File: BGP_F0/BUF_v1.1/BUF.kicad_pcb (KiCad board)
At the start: 2 copper layers, 32 x 26 mm, 33 parts, among them P1 CONN_01X02, P2 CONN_01X02, P3 CONN_01X03, P4 CONN_01X02, P5 CONN_01X09, P6 CONN_01X05, P7 CONN_01X02, Q1 2N5457, Q2 2N5457, U1 MC33178

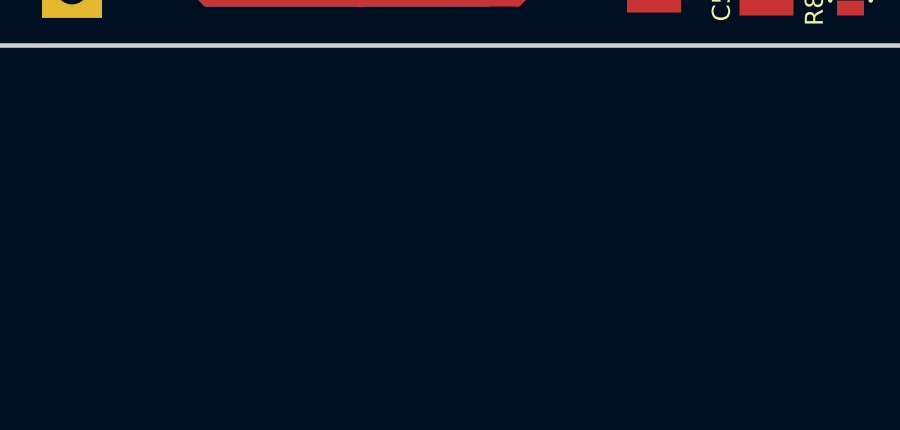
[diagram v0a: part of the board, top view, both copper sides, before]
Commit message: Some changes to names
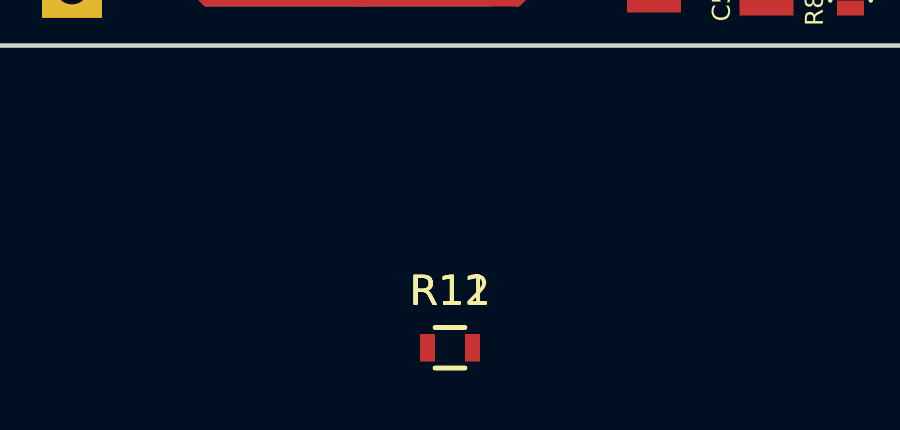
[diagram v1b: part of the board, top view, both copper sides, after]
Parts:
- added R11: 10k, Resistors_SMD:R_0603, F.Cu at (141.0, 114.1)
- added R12: 12k, Resistors_SMD:R_0603, F.Cu at (141.0, 114.1)
- C6: value 100p -> 270p
- R10: value 100 -> 1k
- R5, R6: value 49.9k -> 47k
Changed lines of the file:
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@@
 (kicad_pcb (version 4) (host pcbnew 4.0.4-1.fc24-product)
   (general
-    (links 61)
-    (no_connects 0)
-    (area 123.10412 74.549999 157.175001 104.183001)
+    (links 65)
+    (no_connects 4)
+    (area 124.924999 77.924999 157.075001 104.075001)
     (thickness 1.2)
     (drawings 8)
     (tracks 171)
     (zones 0)
-    (modules 33)
+    (modules 35)
     (nets 25)
   )
@@
       (effects (font (size 0.6 0.6) (thickness 0.15)) (justify mirror))
     )
-    (fp_text value 100p (at 0 -1.9 180) (layer B.Fab) hide
+    (fp_text value 270p (at 0 -1.9 180) (layer B.Fab) hide
       (effects (font (size 0.6 0.6) (thickness 0.15)) (justify mirror))
     )
@@
       (effects (font (size 0.6 0.6) (thickness 0.15)) (justify mirror))
     )
-    (fp_text value 49.9k (at 0 -1.9) (layer B.Fab) hide
+    (fp_text value 47k (at 0 -1.9) (layer B.Fab) hide
       (effects (font (size 0.6 0.6) (thickness 0.15)) (justify mirror))
     )
@@
       (effects (font (size 0.6 0.6) (thickness 0.15)) (justify mirror))
     )
-    (fp_text value 49.9k (at 0 -1.9) (layer B.Fab) hide
+    (fp_text value 47k (at 0 -1.9) (layer B.Fab) hide
       (effects (font (size 0.6 0.6) (thickness 0.15)) (justify mirror))
     )
@@
       (effects (font (size 0.6 0.6) (thickness 0.15)))
     )
-    (fp_text value 100 (at 0 1.9 180) (layer F.Fab) hide
+    (fp_text value 1k (at 0 1.9 180) (layer F.Fab) hide
       (effects (font (size 0.6 0.6) (thickness 0.15)))
     )
@@
     (model Resistors_SMD.3dshapes/R_0603.wrl
       (at (xyz 0 0 0))
+      (scale (xyz 1 1 1))
+      (rotate (xyz 0 0 0))
+    )
+  )
+  (module Resistors_SMD:R_0603 (layer F.Cu)
+    (at 141 114.075001)
+    (descr "Resistor SMD 0603, reflow soldering, Vishay (see dcrcw.pdf)")
+    (tags "resistor 0603")
+    (attr smd)
+    (fp_text reference R11 (at 0 -1.9) (layer F.SilkS)
+      (effects (font (size 1 1) (thickness 0.15)))
+    )
+    (fp_text value 10k (at 0 1.9) (layer F.Fab)
+      (effects (font (size 1 1) (thickness 0.15)))
+    )
+    (fp_line (start -1.3 -0.8) (end 1.3 -0.8) (layer F.CrtYd) (width 0.05))
+    (fp_line (start -1.3 0.8) (end 1.3 0.8) (layer F.CrtYd) (width 0.05))
+    (fp_line (start -1.3 -0.8) (end -1.3 0.8) (layer F.CrtYd) (width 0.05))
+    (fp_line (start 1.3 -0.8) (end 1.3 0.8) (layer F.CrtYd) (width 0.05))
+    (fp_line (start 0.5 0.675) (end -0.5 0.675) (layer F.SilkS) (width 0.15))
+    (fp_line (start -0.5 -0.675) (end 0.5 -0.675) (layer F.SilkS) (width 0.15))
+    (pad 1 smd rect (at -0.75 0) (size 0.5 0.9) (layers F.Cu F.Paste F.Mask)
+      (net 11 /PV_3))
+    (pad 2 smd rect (at 0.75 0) (size 0.5 0.9) (layers F.Cu F.Paste F.Mask)
+      (net 14 /PV_2))
+    (model Resistors_SMD.3dshapes/R_0603.wrl
+      (at (xyz 0 0 0))
+      (scale (xyz 1 1 1))
+      (rotate (xyz 0 0 0))
+    )
+  )
+  (module Resistors_SMD:R_0603 (layer F.Cu)
+    (at 141 114.075001)
+    (descr "Resistor SMD 0603, reflow soldering, Vishay (see dcrcw.pdf)")
+    (tags "resistor 0603")
+    (attr smd)
+    (fp_text reference R12 (at 0 -1.9) (layer F.SilkS)
+      (effects (font (size 1 1) (thickness 0.15)))
+    )
+    (fp_text value 12k (at 0 1.9) (layer F.Fab)
+      (effects (font (size 1 1) (thickness 0.15)))
+    )
+    (fp_line (start -1.3 -0.8) (end 1.3 -0.8) (layer F.CrtYd) (width 0.05))
+    (fp_line (start -1.3 0.8) (end 1.3 0.8) (layer F.CrtYd) (width 0.05))
+    (fp_line (start -1.3 -0.8) (end -1.3 0.8) (layer F.CrtYd) (width 0.05))
+    (fp_line (start 1.3 -0.8) (end 1.3 0.8) (layer F.CrtYd) (width 0.05))
+    (fp_line (start 0.5 0.675) (end -0.5 0.675) (layer F.SilkS) (width 0.15))
+    (fp_line (start -0.5 -0.675) (end 0.5 -0.675) (layer F.SilkS) (width 0.15))
+    (pad 1 smd rect (at -0.75 0) (size 0.5 0.9) (layers F.Cu F.Paste F.Mask)
+      (net 14 /PV_2))
+    (pad 2 smd rect (at 0.75 0) (size 0.5 0.9) (layers F.Cu F.Paste F.Mask)
+      (net 8 Earth))
+    (model Resistors_SMD.3dshapes/R_0603.wrl
+      (at (xyz 0 0 0))

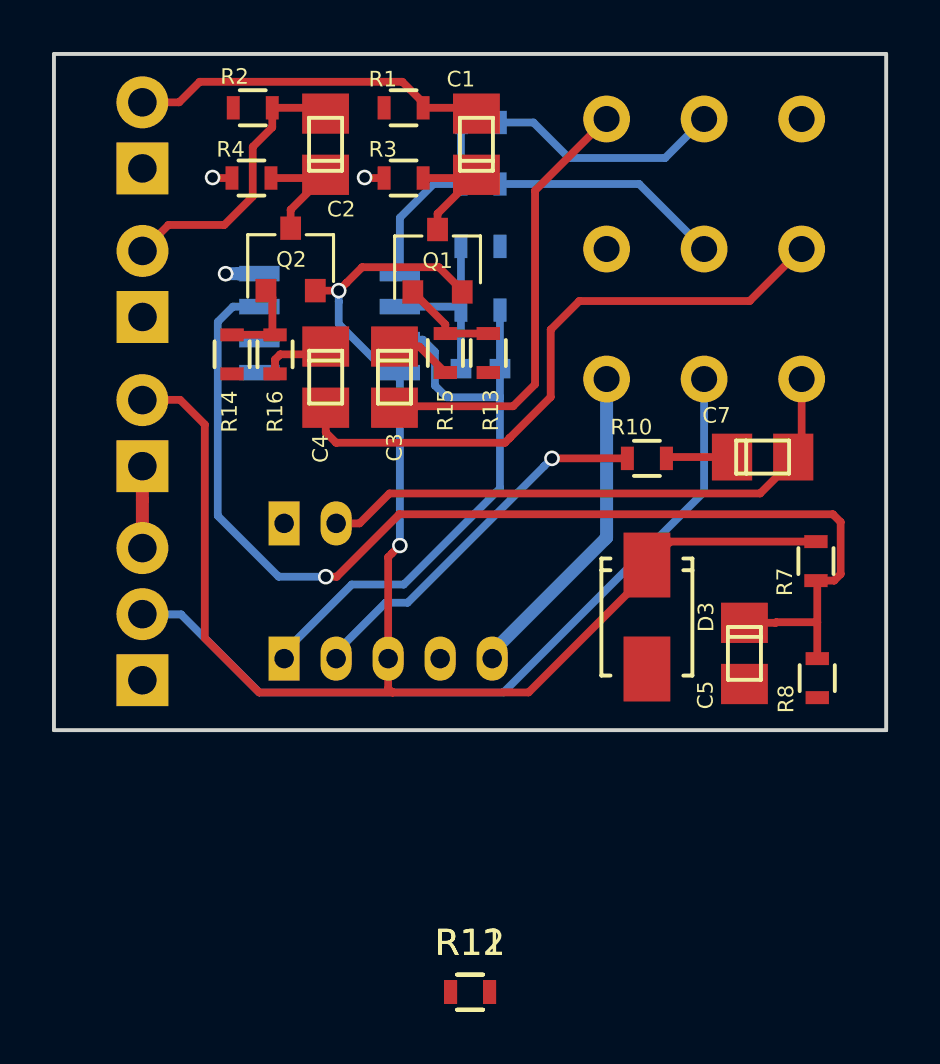
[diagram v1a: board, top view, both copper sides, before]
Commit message: F0 - Fixed Mid Stack, BT, BUF
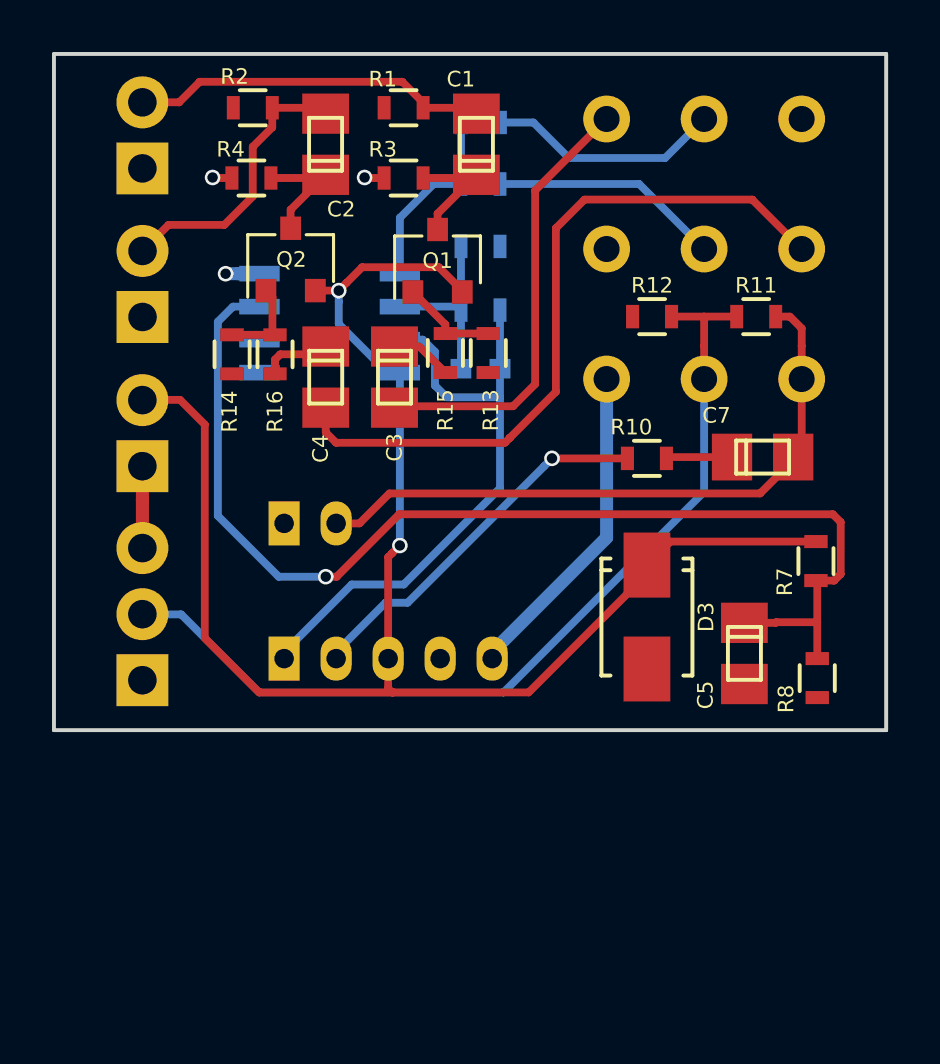
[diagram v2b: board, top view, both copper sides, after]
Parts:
- moved R11 28.2 mm to (152.0, 88.1), turned to 180 degrees
- moved R12 26.9 mm to (148.0, 88.1), turned to 180 degrees
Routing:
- net /PV_2: track 30.4 -> 35.3 mm
- net /PB2_3: track 24.1 -> 27.8 mm
- net /PV_3: track 22.2 -> 25.3 mm
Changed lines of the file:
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@@
-(kicad_pcb (version 4) (host pcbnew 4.0.4-1.fc24-product)
+(kicad_pcb (version 4) (host pcbnew 4.0.7)
   (general
     (links 65)
-    (no_connects 4)
+    (no_connects 0)
     (area 124.924999 77.924999 157.075001 104.075001)
     (thickness 1.2)
     (drawings 8)
-    (tracks 171)
+    (tracks 179)
     (zones 0)
     (modules 35)
@@
     (add_net "Net-(R5-Pad1)")
   )
+  (module Resistors_SMD:R_0603 (layer F.Cu)
+    (at 152 88.1 180)
+    (descr "Resistor SMD 0603, reflow soldering, Vishay (see dcrcw.pdf)")
+    (tags "resistor 0603")
+    (attr smd)
+    (fp_text reference R11 (at 0 1.2 180) (layer F.SilkS)
+      (effects (font (size 0.6 0.6) (thickness 0.15)))
+    )
+    (fp_text value 10k (at 0 1.9 180) (layer F.Fab) hide
+      (effects (font (size 0.6 0.6) (thickness 0.15)))
+    )
+    (fp_line (start -1.3 -0.8) (end 1.3 -0.8) (layer F.CrtYd) (width 0.05))
+    (fp_line (start -1.3 0.8) (end 1.3 0.8) (layer F.CrtYd) (width 0.05))
+    (fp_line (start -1.3 -0.8) (end -1.3 0.8) (layer F.CrtYd) (width 0.05))
+    (fp_line (start 1.3 -0.8) (end 1.3 0.8) (layer F.CrtYd) (width 0.05))
+    (fp_line (start 0.5 0.675) (end -0.5 0.675) (layer F.SilkS) (width 0.15))
+    (fp_line (start -0.5 -0.675) (end 0.5 -0.675) (layer F.SilkS) (width 0.15))
+    (pad 1 smd rect (at -0.75 0 180) (size 0.5 0.9) (layers F.Cu F.Paste F.Mask)
+      (net 11 /PV_3))
+    (pad 2 smd rect (at 0.75 0 180) (size 0.5 0.9) (layers F.Cu F.Paste F.Mask)
+      (net 14 /PV_2))
+    (model Resistors_SMD.3dshapes/R_0603.wrl
+      (at (xyz 0 0 0))
+      (scale (xyz 1 1 1))
+      (rotate (xyz 0 0 0))
+    )
+  )
+  (module Resistors_SMD:R_0603 (layer F.Cu)
+    (at 148 88.1 180)
+    (descr "Resistor SMD 0603, reflow soldering, Vishay (see dcrcw.pdf)")
+    (tags "resistor 0603")
+    (attr smd)
+    (fp_text reference R12 (at 0 1.2 180) (layer F.SilkS)
+      (effects (font (size 0.6 0.6) (thickness 0.15)))
+    )
+    (fp_text value 12k (at 0 1.9 180) (layer F.Fab) hide
+      (effects (font (size 0.6 0.6) (thickness 0.15)))
+    )
+    (fp_line (start -1.3 -0.8) (end 1.3 -0.8) (layer F.CrtYd) (width 0.05))
+    (fp_line (start -1.3 0.8) (end 1.3 0.8) (layer F.CrtYd) (width 0.05))
+    (fp_line (start -1.3 -0.8) (end -1.3 0.8) (layer F.CrtYd) (width 0.05))
+    (fp_line (start 1.3 -0.8) (end 1.3 0.8) (layer F.CrtYd) (width 0.05))
+    (fp_line (start 0.5 0.675) (end -0.5 0.675) (layer F.SilkS) (width 0.15))
+    (fp_line (start -0.5 -0.675) (end 0.5 -0.675) (layer F.SilkS) (width 0.15))
+    (pad 1 smd rect (at -0.75 0 180) (size 0.5 0.9) (layers F.Cu F.Paste F.Mask)
+      (net 14 /PV_2))
+    (pad 2 smd rect (at 0.75 0 180) (size 0.5 0.9) (layers F.Cu F.Paste F.Mask)
+      (net 8 Earth))
+    (model Resistors_SMD.3dshapes/R_0603.wrl
+      (at (xyz 0 0 0))
+      (scale (xyz 1 1 1))
+      (rotate (xyz 0 0 0))
+    )
+  )
   (module LIBS:Potentiometer_Alpha_Tripple_Vertical_Dual_Shaft (layer B.Cu)
     (at 146.25 80.5 90)
@@
     )
   )
-  (module Resistors_SMD:R_0603 (layer F.Cu)
-    (at 141 114.075001)
-    (descr "Resistor SMD 0603, reflow soldering, Vishay (see dcrcw.pdf)")
-    (tags "resistor 0603")
-    (attr smd)
-    (fp_text reference R11 (at 0 -1.9) (layer F.SilkS)
-      (effects (font (size 1 1) (thickness 0.15)))
-    )
-    (fp_text value 10k (at 0 1.9) (layer F.Fab)
-      (effects (font (size 1 1) (thickness 0.15)))
-    )
-    (fp_line (start -1.3 -0.8) (end 1.3 -0.8) (layer F.CrtYd) (width 0.05))
-    (fp_line (start -1.3 0.8) (end 1.3 0.8) (layer F.CrtYd) (width 0.05))
-    (fp_line (start -1.3 -0.8) (end -1.3 0.8) (layer F.CrtYd) (width 0.05))
-    (fp_line (start 1.3 -0.8) (end 1.3 0.8) (layer F.CrtYd) (width 0.05))
-    (fp_line (start 0.5 0.675) (end -0.5 0.675) (layer F.SilkS) (width 0.15))
-    (fp_line (start -0.5 -0.675) (end 0.5 -0.675) (layer F.SilkS) (width 0.15))
-    (pad 1 smd rect (at -0.75 0) (size 0.5 0.9) (layers F.Cu F.Paste F.Mask)
-      (net 11 /PV_3))
-    (pad 2 smd rect (at 0.75 0) (size 0.5 0.9) (layers F.Cu F.Paste F.Mask)
-      (net 14 /PV_2))
-    (model Resistors_SMD.3dshapes/R_0603.wrl
-      (at (xyz 0 0 0))
-      (scale (xyz 1 1 1))
-      (rotate (xyz 0 0 0))
-    )
-  )
-  (module Resistors_SMD:R_0603 (layer F.Cu)
-    (at 141 114.075001)
-    (descr "Resistor SMD 0603, reflow soldering, Vishay (see dcrcw.pdf)")
-    (tags "resistor 0603")
-    (attr smd)
-    (fp_text reference R12 (at 0 -1.9) (layer F.SilkS)
-      (effects (font (size 1 1) (thickness 0.15)))
-    )
-    (fp_text value 12k (at 0 1.9) (layer F.Fab)
-      (effects (font (size 1 1) (thickness 0.15)))
-    )
-    (fp_line (start -1.3 -0.8) (end 1.3 -0.8) (layer F.CrtYd) (width 0.05))
-    (fp_line (start -1.3 0.8) (end 1.3 0.8) (layer F.CrtYd) (width 0.05))
-    (fp_line (start -1.3 -0.8) (end -1.3 0.8) (layer F.CrtYd) (width 0.05))
-    (fp_line (start 1.3 -0.8) (end 1.3 0.8) (layer F.CrtYd) (width 0.05))
-    (fp_line (start 0.5 0.675) (end -0.5 0.675) (layer F.SilkS) (width 0.15))
-    (fp_line (start -0.5 -0.675) (end 0.5 -0.675) (layer F.SilkS) (width 0.15))
-    (pad 1 smd rect (at -0.75 0) (size 0.5 0.9) (layers F.Cu F.Paste F.Mask)
-      (net 14 /PV_2))
-    (pad 2 smd rect (at 0.75 0) (size 0.5 0.9) (layers F.Cu F.Paste F.Mask)
-      (net 8 Earth))
-    (model Resistors_SMD.3dshapes/R_0603.wrl
-      (at (xyz 0 0 0))
-      (scale (xyz 1 1 1))
-      (rotate (xyz 0 0 0))
-    )
-  )
   (gr_line (start 156.7 103.7) (end 156.7 78.3) (layer Margin) (width 0.2))
   (gr_line (start 125.3 103.7) (end 156.7 103.7) (layer Margin) (width 0.2))
@@
   (segment (start 133.5 90.3) (end 133.5 89.75) (width 0.3) (layer F.Cu) (net 5))
   (segment (start 133.5 89.75) (end 133.7 89.55) (width 0.3) (layer F.Cu) (net 5))
-  (segment (start 142.51902 92.770976) (end 144.100011 91.189985) (width 0.3) (layer F.Cu) (net 6))
-  (segment (start 144.100011 91.189985) (end 144.100011 88.599989) (width 0.3) (layer F.Cu) (net 6))
-  (segment (start 144.100011 88.599989) (end 145.2 87.5) (width 0.3) (layer F.Cu) (net 6))
-  (segment (start 145.2 87.5) (end 151.75 87.5) (width 0.3) (layer F.Cu) (net 6))
-  (segment (start 151.75 87.5) (end 153.75 85.5) (width 0.3) (layer F.Cu) (net 6))
+  (segment (start 144.3 84.7) (end 144.3 90.989996) (width 0.3) (layer F.Cu) (net 6))
+  (segment (start 144.3 90.989996) (end 142.51902 92.770976) (width 0.3) (layer F.Cu) (net 6))
+  (segment (start 145.4 83.6) (end 144.3 84.7) (width 0.3) (layer F.Cu) (net 6))
+  (segment (start 151.85 83.6) (end 145.4 83.6) (width 0.3) (layer F.Cu) (net 6))
+  (segment (start 153.75 85.5) (end 151.85 83.6) (width 0.3) (layer F.Cu) (net 6))
   (segment (start 135.45 91.57602) (end 135.45 92.55) (width 0.3) (layer F.Cu) (net 6))
   (segment (start 142.51902 92.770976) (end 142.539998 92.749998) (width 0.3) (layer F.Cu) (net 6))
@@
   (segment (start 151.07398 93.5) (end 148.6 93.5) (width 0.3) (layer F.Cu) (net 10))
   (segment (start 148.6 93.5) (end 148.55 93.55) (width 0.3) (layer F.Cu) (net 10))
+  (segment (start 152.75 88.1) (end 153.3 88.1) (width 0.3) (layer F.Cu) (net 11))
+  (segment (start 153.3 88.1) (end 153.75 88.55) (width 0.3) (layer F.Cu) (net 11))
+  (segment (start 153.75 88.55) (end 153.75 89.227208) (width 0.3) (layer F.Cu) (net 11))
+  (segment (start 153.75 89.227208) (end 153.75 90.5) (width 0.3) (layer F.Cu) (net 11))
   (segment (start 153.75 90.5) (end 153.75 93.17602) (width 0.3) (layer F.Cu) (net 11))
   (segment (start 153.75 93.17602) (end 153.42602 93.5) (width 0.3) (layer F.Cu) (net 11))
@@
   (segment (start 139.193993 80.070255) (end 141.020013 80.070255) (width 0.3) (layer F.Cu) (net 13))
   (segment (start 141.020013 80.070255) (end 141.243993 80.294235) (width 0.3) (layer F.Cu) (net 13))
+  (segment (start 150 88.1) (end 151.25 88.1) (width 0.3) (layer F.Cu) (net 14))
+  (segment (start 148.75 88.1) (end 150 88.1) (width 0.3) (layer F.Cu) (net 14))
+  (segment (start 150 90.5) (end 150 89.227208) (width 0.3) (layer F.Cu) (net 14))
+  (segment (start 150 89.227208) (end 150 88.1) (width 0.3) (layer F.Cu) (net 14))
   (segment (start 128.4 99.54) (end 128.41 99.55) (width 0.3) (layer B.Cu) (net 14))
   (segment (start 142.284928 102.55001) (end 150 94.834938) (width 0.3) (layer B.Cu) (net 14))

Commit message: F0 BUF changed rotation
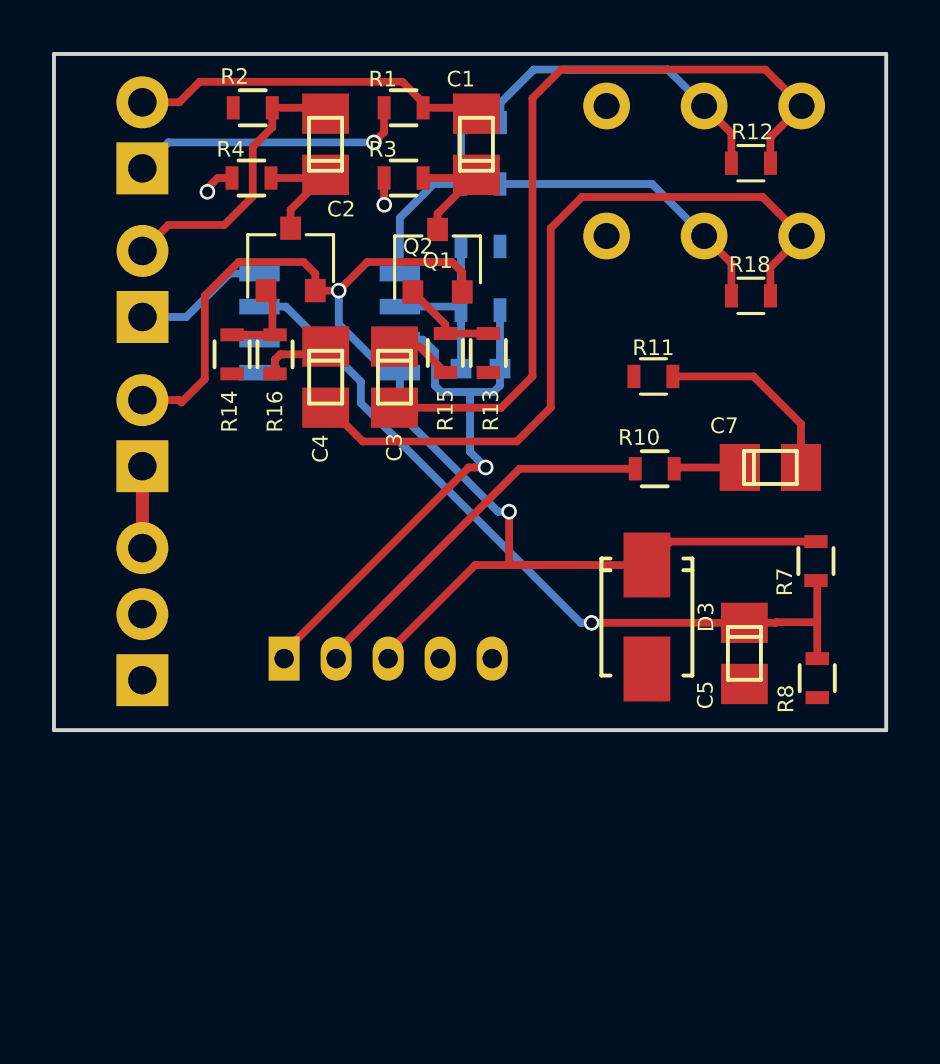
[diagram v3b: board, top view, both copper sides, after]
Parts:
- removed P7: CONN_01X02, Connectors_JST:JST_PH_B2B-PH-K_02x2.00mm_Straight
- added R18: 12k, Resistors_SMD:R_0603, F.Cu at (151.8, 87.3)
- P5: value CONN_01X09 -> Conn_01x06; footprint LIBS:Potentiometer_Alpha_Tripple_Vertical_Dual_Shaft -> LIBS:Potentiometer_Alpha_Double_Vertical_Dual_Shaft
- R11: value 10k -> 20k
- R5, R6: value 47k -> 4.7k
- moved R12 7.02 mm to (151.8, 82.2), turned to 0 degrees
- moved R11 4.57 mm to (148.1, 90.4)
- moved C7 0.50 mm to (152.6, 93.9)
- moved P5 0.50 mm to (146.2, 80.0)
- moved R10 0.50 mm to (148.1, 94.0)
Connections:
- net /PB2_3 renamed /PB2_1
- C7 pad 2: /PV_3 -> Net-(C7-Pad2)
- P5 pad 1: /PB1_1 -> /VRef
- P5 pad 3: /VRef -> /PB1_1
- R11 pad 1: /PV_3 -> Net-(C7-Pad2)
- R11 pad 2: /PV_2 -> Earth
- R12 pad 1: /PV_2 -> /PB1_2
- R12 pad 2: Earth -> /PB1_1
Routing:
- net /PV_2: track 35.3 -> 0.01 mm
- net /PV_3: track 25.3 -> 0.00 mm
- net Net-(C5-Pad1): track 44.0 -> 30.1 mm
- net /PB1_1: track 17.1 -> 30.7 mm
- net Net-(C7-Pad2): track 0.00 -> 8.26 mm
- net /V+: track 61.7 -> 54.0 mm
- net /PB1_2: track 9.02 -> 12.3 mm
- net /PB2_2: track 8.89 -> 11.4 mm
- net /PB2_1: track 27.8 -> 30.2 mm
- net Earth: track 13.9 -> 16.0 mm
- net /IN_EQ: track 23.6 -> 22.8 mm, vias 0 -> 1
- net /VRef: track 1.51 -> 2.33 mm
- net /OUT_EQ: track 14.5 -> 14.9 mm, vias 1 -> 0
